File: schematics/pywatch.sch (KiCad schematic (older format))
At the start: 9 parts

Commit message: added a few connections
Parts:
- added BT?: Battery_Cell, symbol Device:Battery_Cell
- added U?: LM27313XMF, Package_TO_SOT_SMD:SOT-23-5, symbol Regulator_Switching:LM27313XMF
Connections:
- net +5V: now also P?.B5 (VCONN)
- net GND: now also P?.S1 (SHIELD), U?.2 (GND)
- net +3V3: now reaches U?.4 (V3)
- net at U?.6 (BAT): now also U?.3 (VBAT), BT?.1 (+), U?.4 (EN), U?.5 (VIN)
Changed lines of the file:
@@
 EESchema Schematic File Version 4
+LIBS:pywatch-cache
 EELAYER 29 0
 EELAYER END
@@
 Wire Wire Line
 	3050 4600 3050 4500
+$Comp
+L power:+3V3 #PWR?
+U 1 1 5D2B0EF1
+P 2950 4500
+F 0 "#PWR?" H 2950 4350 50  0001 C CNN
+F 1 "+3V3" H 2965 4673 50  0000 C CNN
+F 2 "" H 2950 4500 50  0001 C CNN
+F 3 "" H 2950 4500 50  0001 C CNN
+	1    2950 4500
+	1    0    0    -1
+$EndComp
+Wire Wire Line
+	2950 4500 2950 4600
+$Comp
+L Device:Battery_Cell BT?
+U 1 1 5D2B406E
+P 4250 3800
+F 0 "BT?" H 4368 3896 50  0000 L CNN
+F 1 "Battery_Cell" H 4368 3805 50  0000 L CNN
+F 2 "" V 4250 3860 50  0001 C CNN
+F 3 "~" V 4250 3860 50  0001 C CNN
+	1    4250 3800
+	1    0    0    -1
+$EndComp
+$Comp
+L Regulator_Switching:LM27313XMF U?
+U 1 1 5D2B5911
+P 4050 2550
+F 0 "U?" H 4050 2917 50  0000 C CNN
+F 1 "LM27313XMF" H 4050 2826 50  0000 C CNN
+F 2 "Package_TO_SOT_SMD:SOT-23-5" H 4100 2300 50  0001 L CIN
+F 3 "http://www.ti.com/lit/ds/symlink/lm27313.pdf" H 4050 2650 50  0001 C CNN
+	1    4050 2550
+	1    0    0    -1
+$EndComp
+Wire Wire Line
+	3400 3300 3600 3300
+Wire Wire Line
+	4250 3300 4250 3600
+Wire Wire Line
+	3600 3300 3600 2650
+Wire Wire Line
+	3600 2450 3750 2450
+Connection ~ 3600 3300
+Wire Wire Line
+	3600 3300 4250 3300
+Wire Wire Line
+	3600 2650 3750 2650
+Connection ~ 3600 2650
+Wire Wire Line
+	3600 2650 3600 2450
+$Comp
+L power:GND #PWR?
+U 1 1 5D2C566B
+P 4050 3050
+F 0 "#PWR?" H 4050 2800 50  0001 C CNN
+F 1 "GND" H 4055 2877 50  0000 C CNN
+F 2 "" H 4050 3050 50  0001 C CNN
+F 3 "" H 4050 3050 50  0001 C CNN
+	1    4050 3050
+	1    0    0    -1
+$EndComp
+Wire Wire Line
+	4050 3050 4050 2850
+$Comp
+L power:+5V #PWR?
+U 1 1 5D2C86B1
+P 4650 2150
+F 0 "#PWR?" H 4650 2000 50  0001 C CNN
+F 1 "+5V" H 4665 2323 50  0000 C CNN
+F 2 "" H 4650 2150 50  0001 C CNN
+F 3 "" H 4650 2150 50  0001 C CNN
+	1    4650 2150
+	1    0    0    -1
+$EndComp
+Wire Wire Line
+	4250 3300 5300 3300
+Wire Wire Line
+	5300 3300 5300 1400
+Wire Wire Line
+	5300 1400 5700 1400
+Connection ~ 4250 3300
+Wire Wire Line
+	1650 4950 1750 4950
+Wire Wire Line
+	1750 4950 1750 4650
+Wire Wire Line
+	750  6150 1050 6150
+Connection ~ 1050 6150
 $EndSCHEMATC

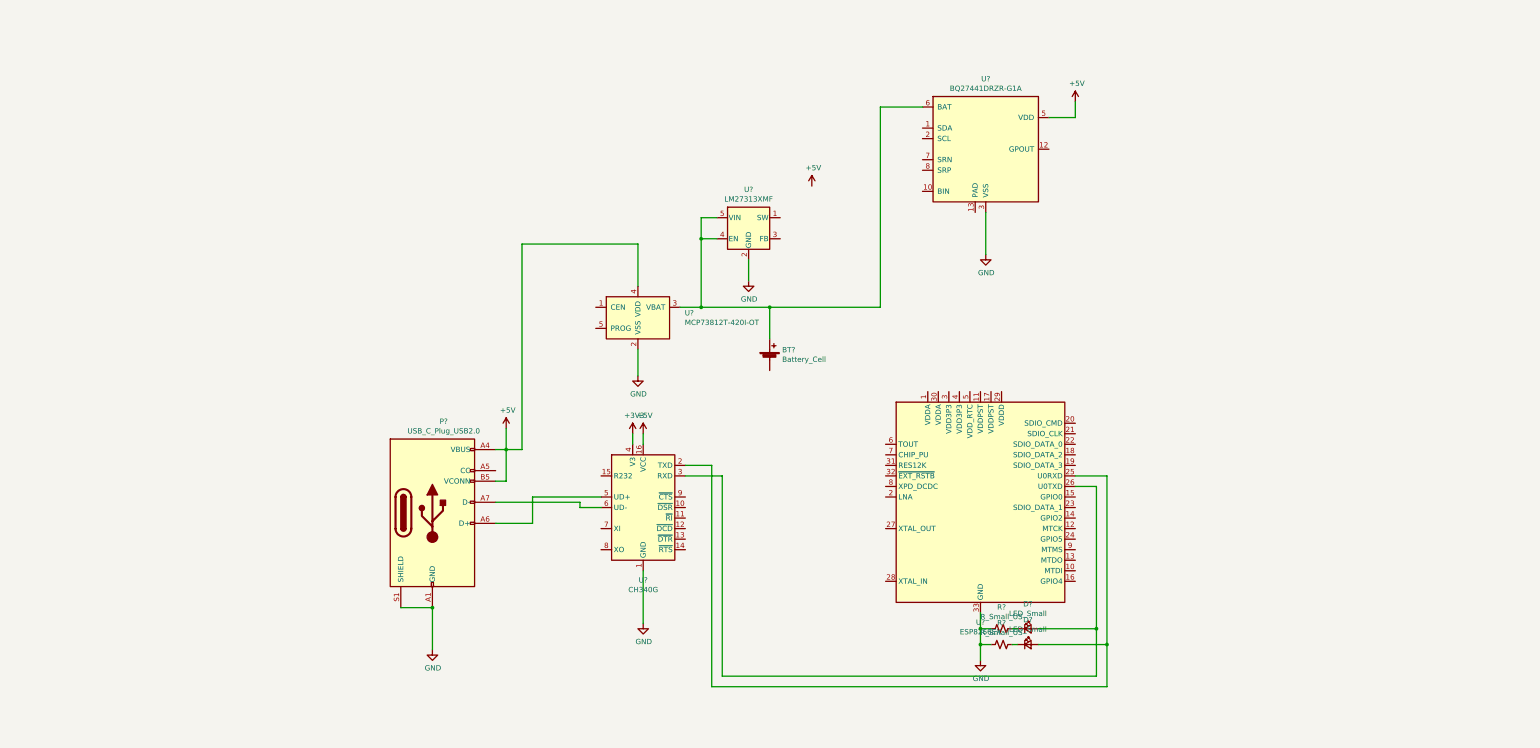
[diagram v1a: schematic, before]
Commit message: added majority of circuit
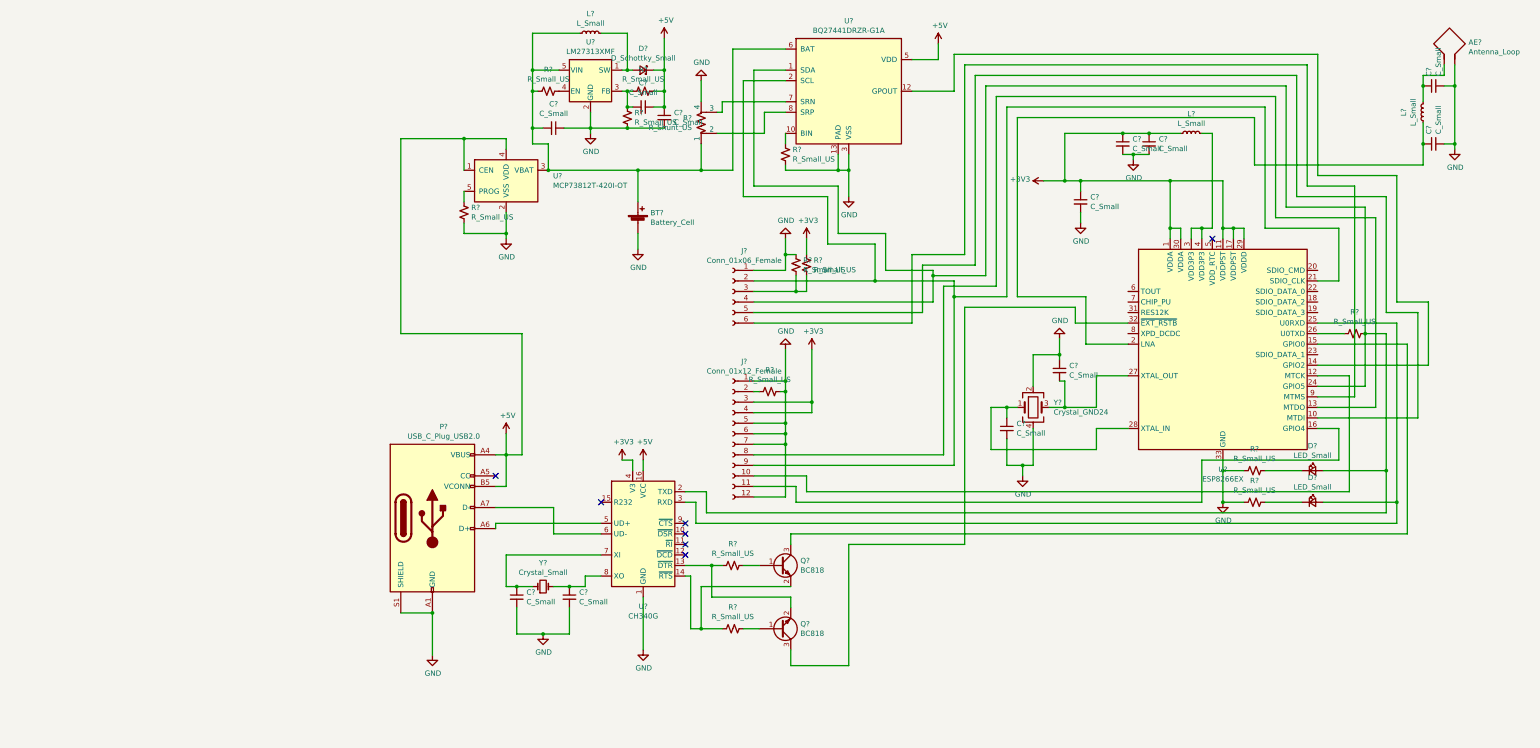
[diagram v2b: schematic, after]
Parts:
- added AE?: Antenna_Loop, symbol Device:Antenna_Loop
- added C? (x12): C_Small, symbol Device:C_Small
- added D?: D_Schottky_Small, symbol Device:D_Schottky_Small
- added J?: Conn_01x06_Female, symbol Connector:Conn_01x06_Female
- added J?: Conn_01x12_Female, symbol Connector:Conn_01x12_Female
- added L? (x3): L_Small, symbol Device:L_Small
- added Q? (x2): BC818, Package_TO_SOT_SMD:SOT-23, symbol Transistor_BJT:BC818
- added R? (x11): R_Small_US, symbol Device:R_Small_US
- added R?: R_Shunt_US, symbol Device:R_Shunt_US
- added Y?: Crystal_GND24, symbol Device:Crystal_GND24
- added Y?: Crystal_Small, symbol Device:Crystal_Small
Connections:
- net +3V3: now also U?.1 (VDDA), U?.11 (VDDPST), U?.17 (VDDPST), U?.29 (VDDD), U?.30 (VDDA), C?.1, C?.1, C?.1, J?.3 (Pin_3), J?.4 (Pin_4), L?.2, R?.2
- net +5V: now also U?.1 (CEN), C?.1, C?.1, D?.1 (K), R?.1
- net GND: now also BT?.2 (-), U?.13 (PAD), AE?.2, C?.1, C?.1, C?.2, C?.2, C?.2, C?.2, C?.2, C?.2, C?.2, C?.2, C?.2, J?.1 (Pin_1), J?.1 (Pin_1), J?.12 (Pin_12), J?.5 (Pin_5), J?.6 (Pin_6), J?.7 (Pin_7), R?.1, R?.1, R?.2, R?.2, R?.2, R?.4, Y?.2, Y?.4
- net at U?.10 (MTDI): now also J?.5 (Pin_5)
- net at U?.12 (MTCK): now also J?.10 (Pin_10)
- net at U?.13 (MTDO): now also J?.8 (Pin_8)
- net at U?.14 (GPIO2): now also U?.12 (GPOUT)
- net at U?.15 (GPIO0): now also Q?.3 (C)
- net at U?.16 (GPIO4): now also J?.11 (Pin_11)
- net at U?.2 (LNA): now also C?.1, L?.2
- net at U?.21 (SDIO_CLK): now also U?.2 (SCL), J?.2 (Pin_2), J?.9 (Pin_9)
- net at U?.24 (GPIO5): now also D?.2 (A), U?.1 (SDA), U?.2 (TXD), J?.4 (Pin_4), R?.2
- net at D?.2 (A), U?.25 (U0RXD): now also U?.3 (RXD); no longer U?.2 (TXD)
- net at U?.27 (XTAL_OUT): now also C?.2, Y?.3
- net at U?.28 (XTAL_IN): now also C?.1, Y?.1
- net at U?.3 (VDD3P3): now also U?.4 (VDD3P3), L?.1
- net at U?.32 (~EXT_RSTB~): now also Q?.3 (C)
- net at U?.9 (MTMS): now also J?.6 (Pin_6)
- net at U?.13 (~DTR): now also Q?.2 (E), R?.2
- net at U?.14 (~RTS): now also Q?.2 (E), R?.2
- net at U?.7 (XI): now also C?.1, Y?.1
- net at U?.8 (XO): now also C?.1, Y?.2
- net at U?.10 (BIN): now also R?.1
- net at BT?.1 (+), U?.3 (VBAT), U?.5 (VIN)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: now also C?.2, L?.2, R?.1, R?.2; no longer U?.4 (EN)
- net at U?.7 (SRN): now also R?.3
- net at U?.8 (SRP): now also R?.2
- net at U?.1 (SW): now also D?.2 (A), L?.1
- net at U?.3 (FB): now also C?.2, R?.2, R?.2
- net at U?.5 (PROG): now also R?.1
- new net: R?.1, U?.26 (U0TXD)
- new net: R?.1, U?.4 (EN)
- new net: Q?.1 (B), R?.1 (x2)
- new net: J?.3 (Pin_3), R?.1, R?.1
- new net: J?.2 (Pin_2), R?.2
- new net: AE?.1, C?.1, L?.1
- no-connect marks 0 -> 7
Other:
- moved on the sheet: BT?, D?, P?, R?, U?

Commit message: completed schematic
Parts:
- added U?: AT25DF041x-UxN-x, Package_CSP:WLCSP-8_1.58x1.63x0.35mm_Layout3x5_P0.35x0.4mm_Ball0.25mm_Pad0.25mm_NSMD, symbol Memory_Flash:AT25DF041x-UxN-x
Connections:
- net +3V3: now also U?.7 (CHIP_PU), U?.A1 (VCC)
- net GND: now also U?.B2 (GND)
- net at U?.18 (SDIO_DATA_2): now also U?.C1 (~HOLD~)
- net at U?.19 (SDIO_DATA_3): now also U?.E3 (~WP~)
- net at U?.20 (SDIO_CMD): now also U?.A3 (~CS)
- net at J?.2 (Pin_2), J?.9 (Pin_9), U?.2 (SCL)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: now also U?.E1 (SCK)
- net at U?.22 (SDIO_DATA_0): now also U?.C3 (SO/IO1)
- net at U?.23 (SDIO_DATA_1): now also U?.D2 (SI/IO0)
- net at Q?.3 (C), U?.32 (~EXT_RSTB~): now also U?.8 (XPD_DCDC)
- no-connect marks 7 -> 9
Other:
- moved on the sheet: Q?, R?

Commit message: added boundry boxes to sch
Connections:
- no-connect marks 9 -> 10
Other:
- note added: "Antenna"
- note added: "Battery Charge\n& Power Electronics"
- note added: "Flash Memory"
- note added: "Micro Processor"
- note added: "Screen &\nTouch IO"
- note added: "USB Interface"
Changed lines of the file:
@@
 NoConn ~ 7650 3350
 NoConn ~ 7650 3150
+NoConn ~ -2950 5850
+Wire Notes Line
+	3650 2800 3650 2300
+Wire Notes Line
+	3650 2300 4750 2300
+Wire Notes Line
+	4750 2650 5600 2650
+Wire Notes Line
+	5600 2650 5600 600
+Wire Notes Line
+	5600 600  550  600
+Wire Notes Line
+	550  2800 550  600
+Wire Notes Line
+	2100 2800 2100 4650
+Wire Notes Line
+	2100 4650 3800 4650
+Wire Notes Line
+	550  2800 3800 2800
+Wire Notes Line
+	2100 4300 550  4300
+Wire Notes Line
+	550  4300 550  6850
+Wire Notes Line
+	550  6850 3350 6850
+Wire Notes Line
+	3350 6850 3350 7400
+Wire Notes Line
+	5100 7400 5100 6200
+Wire Notes Line
+	5100 6200 3800 6200
+Wire Notes Line
+	3800 2800 3800 6200
+Wire Notes Line
+	3350 7400 5100 7400
+Wire Notes Line
+	4750 5200 3800 5200
+Wire Notes Line
+	4750 2300 4750 5200
+Wire Notes Line
+	5950 5700 10550 5700
+Wire Notes Line
+	10550 5700 10550 4600
+Wire Notes Line
+	10550 4600 10650 4600
+Wire Notes Line
+	10650 4600 10650 4100
+Wire Notes Line
+	10650 4100 10750 4100
+Wire Notes Line
+	10750 4100 10750 2600
+Wire Notes Line
+	10750 2600 9500 2600
+Wire Notes Line
+	9500 2600 9500 850
+Wire Notes Line
+	9500 850  5950 850
+Wire Notes Line
+	5950 850  5950 5700
+Wire Notes Line
+	10150 600  11050 600
+Wire Notes Line
+	11050 600  11050 2000
+Wire Notes Line
+	11050 2000 10150 2000
+Wire Notes Line
+	10150 2000 10150 600
+Text Notes 600  900  0    79   ~ 0
+Battery Charge\n& Power Electronics
+Text Notes 2600 4350 0    79   ~ 0
+Flash Memory
+Text Notes 1350 6800 0    79   ~ 0
+USB Interface
+Text Notes 7000 5000 0    79   ~ 0
+Micro Processor
+Text Notes 10150 700  0    79   ~ 0
+Antenna
+Text Notes 3750 2650 0    79   ~ 0
+Screen &\nTouch IO
 $EndSCHEMATC

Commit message: started pcb design
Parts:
- AE1: renamed from AE?; footprint (none) -> RF_Antenna:Texas_SWRA117D_2.4GHz_Right
- C1, C10, C11, C12, C2, C3, C4, C5, C6, C7, C8, C9: renamed from C?; footprint (none) -> Capacitor_SMD:C_1206_3216Metric_Pad1.42x1.75mm_HandSolder
- D1: renamed from D?; footprint (none) -> Diode_SMD:D_1206_3216Metric_Pad1.42x1.75mm_HandSolder
- D2, D3: renamed from D?; footprint (none) -> LED_SMD:LED_1206_3216Metric_Pad1.42x1.75mm_HandSolder
- J1: renamed from J?; footprint (none) -> Connector_FFC-FPC:Molex_200528-0060_1x06-1MP_P1.00mm_Horizontal
- J2: renamed from J?; footprint (none) -> Connector_FFC-FPC:Molex_200528-0120_1x12-1MP_P1.00mm_Horizontal
- L1, L2, L3: renamed from L?; footprint (none) -> Inductor_SMD:L_1206_3216Metric_Pad1.42x1.75mm_HandSolder
- P1: renamed from P?; footprint (none) -> Connector_USB:USB_C_Plug_Molex_105444
- R1, R10, R11, R12, R13, R14, R2, R3, R4, R5, R6, R7, R8, R9: renamed from R?; footprint (none) -> Resistor_SMD:R_1206_3216Metric_Pad1.42x1.75mm_HandSolder
- U3: renamed from U?; footprint Package_CSP:WLCSP-8_1.58x1.63x0.35mm_Layout3x5_P0.35x0.4mm_Ball0.25mm_Pad0.25mm_NSMD -> Package_TO_SOT_SMD:SOT-223-8
- Y1: renamed from Y?; footprint (none) -> Crystal:Crystal_SMD_HC49-SD_HandSoldering
- Y2: renamed from Y?; footprint (none) -> Crystal:Crystal_SMD_SeikoEpson_FA238-4Pin_3.2x2.5mm_HandSoldering
- gave numbers to parts that had none: 8
